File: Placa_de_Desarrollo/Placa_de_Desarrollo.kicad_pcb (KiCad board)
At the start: 2 copper layers, 1 part, among them U1 Pico

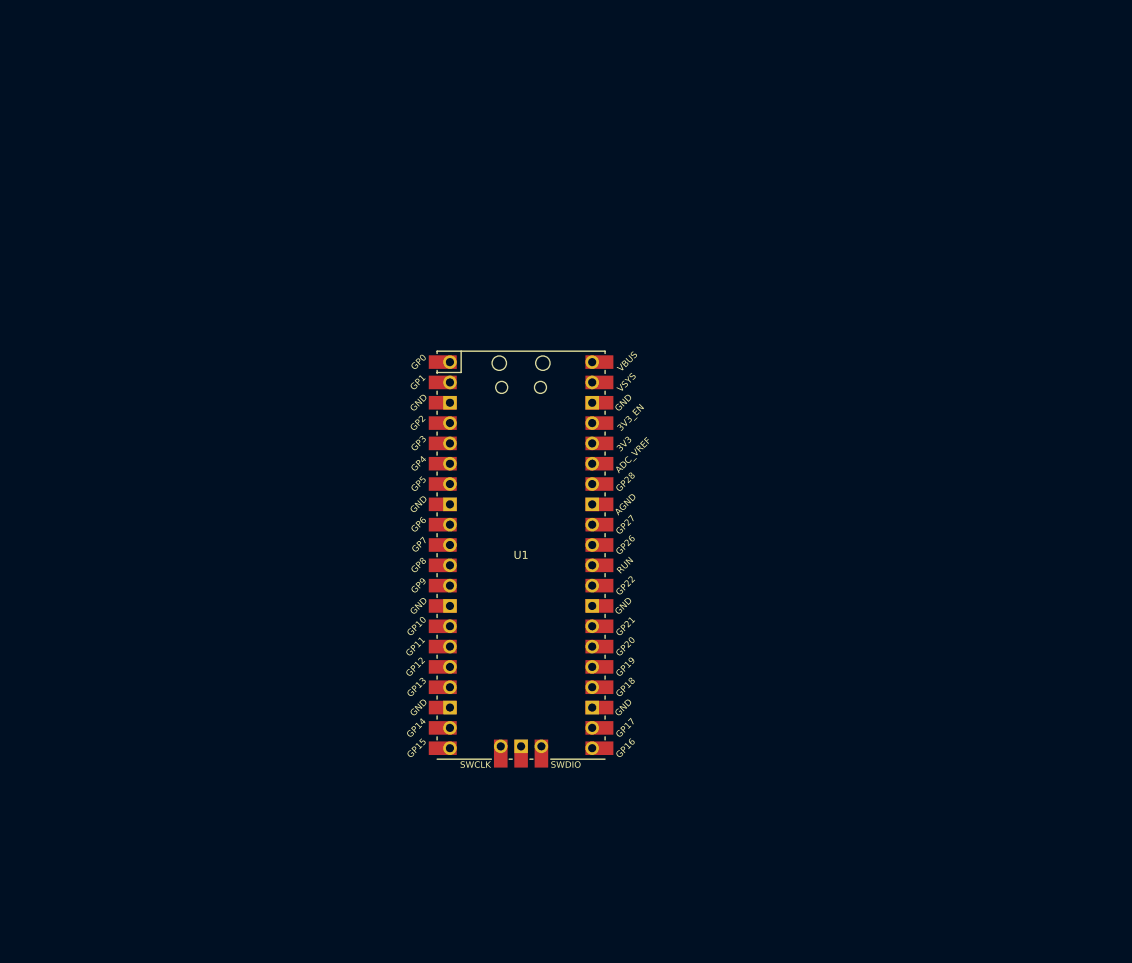
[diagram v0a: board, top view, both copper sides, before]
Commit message: Cambio de huella del Buzzer
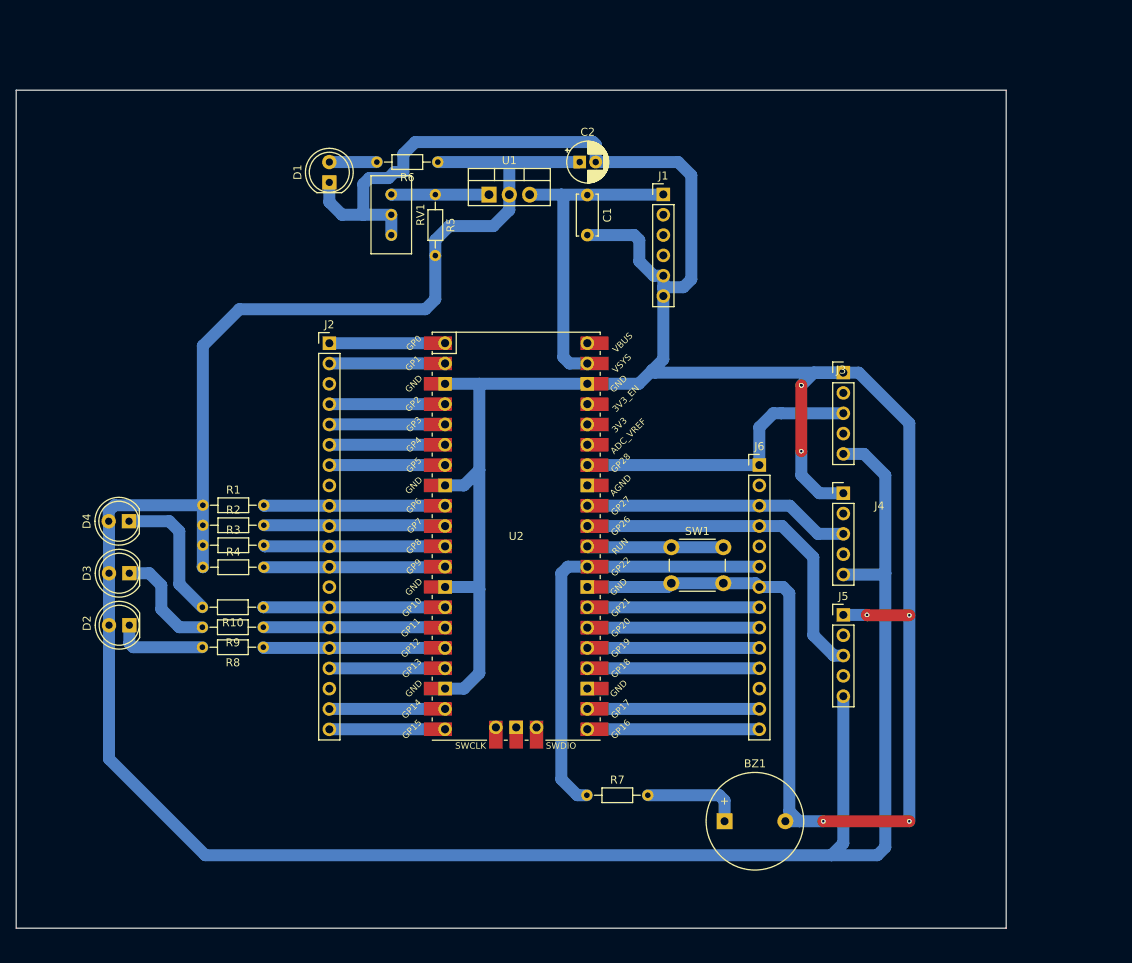
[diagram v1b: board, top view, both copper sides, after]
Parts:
- added BZ1: Buzzer, Buzzer_Beeper:Buzzer_12x9.5RM7.6, F.Cu at (172.0, 125.6)
- added C1: 0.1uF, Capacitor_THT:C_Disc_D5.0mm_W2.5mm_P5.00mm, F.Cu at (154.9, 47.4)
- added C2: 10uF, Capacitor_THT:CP_Radial_D5.0mm_P2.00mm, F.Cu at (153.9, 43.2)
- added D1: LED, LED_THT:LED_D5.0mm, F.Cu at (122.6, 45.8)
- added D2: LED, LED_THT:LED_D5.0mm, F.Cu at (97.6, 101.1)
- added D3: LED, LED_THT:LED_D5.0mm, F.Cu at (97.6, 94.6)
- added D4: LED, LED_THT:LED_D5.0mm, F.Cu at (97.6, 88.1)
- added J1: USB_B_Micro, Connector_PinHeader_2.54mm:PinHeader_1x06_P2.54mm_Vertical, F.Cu at (164.4, 47.3)
- added J2: Conn_01x20, Connector_PinHeader_2.54mm:PinHeader_1x20_P2.54mm_Vertical, F.Cu at (122.6, 65.9)
- added J3: ADC0, Connector_PinHeader_2.54mm:PinHeader_1x05_P2.54mm_Vertical, F.Cu at (186.9, 69.6)
- added J4: ADC1, Connector_PinHeader_2.54mm:PinHeader_1x05_P2.54mm_Vertical, F.Cu at (186.9, 84.6)
- added J5: ADC2, Connector_PinHeader_2.54mm:PinHeader_1x05_P2.54mm_Vertical, F.Cu at (186.9, 99.8)
- added J6: Conn_01x14, Connector_PinHeader_2.54mm:PinHeader_1x14_P2.54mm_Vertical, F.Cu at (176.4, 81.1)
- added R1: 4,7k, Resistor_THT:R_Axial_DIN0204_L3.6mm_D1.6mm_P7.62mm_Horizontal, F.Cu at (106.8, 86.1)
- added R10: 220, Resistor_THT:R_Axial_DIN0204_L3.6mm_D1.6mm_P7.62mm_Horizontal, F.Cu at (114.4, 98.9)
- added R2: 4,7k, Resistor_THT:R_Axial_DIN0204_L3.6mm_D1.6mm_P7.62mm_Horizontal, F.Cu at (106.8, 88.6)
- added R3: 4,7k, Resistor_THT:R_Axial_DIN0204_L3.6mm_D1.6mm_P7.62mm_Horizontal, F.Cu at (106.8, 91.1)
- added R4: 4,7k, Resistor_THT:R_Axial_DIN0204_L3.6mm_D1.6mm_P7.62mm_Horizontal, F.Cu at (106.8, 93.9)
- added R5: 240, Resistor_THT:R_Axial_DIN0204_L3.6mm_D1.6mm_P7.62mm_Horizontal, F.Cu at (135.9, 47.3)
- added R6: 240, Resistor_THT:R_Axial_DIN0204_L3.6mm_D1.6mm_P7.62mm_Horizontal, F.Cu at (136.2, 43.2)
- added R7: 100, Resistor_THT:R_Axial_DIN0204_L3.6mm_D1.6mm_P7.62mm_Horizontal, F.Cu at (154.8, 122.4)
- added R8: 220, Resistor_THT:R_Axial_DIN0204_L3.6mm_D1.6mm_P7.62mm_Horizontal, F.Cu at (114.4, 103.9)
- added R9: 220, Resistor_THT:R_Axial_DIN0204_L3.6mm_D1.6mm_P7.62mm_Horizontal, F.Cu at (114.4, 101.4)
- added RV1: 1K, Potentiometer_THT:Potentiometer_Bourns_3296W_Vertical, F.Cu at (130.4, 52.4)
- added SW1: RESET, Button_Switch_THT:SW_PUSH_6mm_H9.5mm, F.Cu at (165.4, 91.4)
- added U1: LM317_TO-220, Package_TO_SOT_THT:TO-220-3_Vertical, F.Cu at (142.6, 47.3)
- moved U2 2.45 mm to (146.0, 90.0)
- renumbered U1 to U2
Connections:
- U2 pad 1: unconnected-(U1-GPIO0-Pad1) -> GPIO0/SCK
- U2 pad 10: unconnected-(U1-GPIO7-Pad10) -> SCL1
- U2 pad 11: unconnected-(U1-GPIO8-Pad11) -> SDA0
- U2 pad 12: unconnected-(U1-GPIO9-Pad12) -> SCL0
- U2 pad 13: unconnected-(U1-GND-Pad13) -> GND
- U2 pad 14: unconnected-(U1-GPIO10-Pad14) -> LED1
- U2 pad 15: unconnected-(U1-GPIO11-Pad15) -> LED2
- U2 pad 16: unconnected-(U1-GPIO12-Pad16) -> LED3
- U2 pad 17: unconnected-(U1-GPIO13-Pad17) -> GPIO13
- U2 pad 18: unconnected-(U1-GND-Pad18) -> GND
- U2 pad 19: unconnected-(U1-GPIO14-Pad19) -> F1/GPIO14
- U2 pad 2: unconnected-(U1-GPIO1-Pad2) -> GPIO1/TX
- U2 pad 20: unconnected-(U1-GPIO15-Pad20) -> F2/GPIO15
- U2 pad 21: unconnected-(U1-GPIO16-Pad21) -> F3/GPIO16
- U2 pad 22: unconnected-(U1-GPIO17-Pad22) -> F4/GPIO17
- U2 pad 23: unconnected-(U1-GND-Pad23) -> GND
- U2 pad 24: unconnected-(U1-GPIO18-Pad24) -> C1/GPIO18
- U2 pad 25: unconnected-(U1-GPIO19-Pad25) -> C2/GPIO19
- U2 pad 26: unconnected-(U1-GPIO20-Pad26) -> C3/GPIO20
- U2 pad 27: unconnected-(U1-GPIO21-Pad27) -> C4/GPIO21
- U2 pad 28: unconnected-(U1-GND-Pad28) -> GND
- U2 pad 29: unconnected-(U1-GPIO22-Pad29) -> BUZZER
- U2 pad 3: unconnected-(U1-GND-Pad3) -> GND
- U2 pad 30: unconnected-(U1-RUN-Pad30) -> Net-(U2-RUN)
- U2 pad 31: unconnected-(U1-GPIO26_ADC0-Pad31) -> ADC0
- U2 pad 32: unconnected-(U1-GPIO27_ADC1-Pad32) -> ADC1
- U2 pad 34: unconnected-(U1-GPIO28_ADC2-Pad34) -> ADC2
- U2 pad 38: unconnected-(U1-GND-Pad38) -> GND
- U2 pad 39: unconnected-(U1-VSYS-Pad39) -> 5V
- U2 pad 4: unconnected-(U1-GPIO2-Pad4) -> GPIO2/RX
- U2 pad 5: unconnected-(U1-GPIO3-Pad5) -> GPIO3/CSn
- U2 pad 6: unconnected-(U1-GPIO4-Pad6) -> GPIO4
- U2 pad 7: unconnected-(U1-GPIO5-Pad7) -> GPIO5
- U2 pad 8: unconnected-(U1-GND-Pad8) -> GND
- U2 pad 9: unconnected-(U1-GPIO6-Pad9) -> SDA1
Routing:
- net GND: track 0.00 -> 371.3 mm, vias 0 -> 7
- net 3.3V: track 0.00 -> 325.3 mm
- net BUZZER: track 0.00 -> 54.9 mm
- net ADC0: track 0.00 -> 44.4 mm
- net 5V: track 0.00 -> 40.5 mm
- net ADC2: track 0.00 -> 37.5 mm
- net ADC1: track 0.00 -> 33.5 mm
- net LED3: track 0.00 -> 22.8 mm
- net LED2: track 0.00 -> 22.7 mm
- net LED1: track 0.00 -> 22.7 mm
- net SDA0: track 0.00 -> 22.7 mm
- net SCL1: track 0.00 -> 22.7 mm
- net SCL0: track 0.00 -> 22.7 mm
- net SDA1: track 0.00 -> 22.7 mm
- net C4/GPIO21: track 0.00 -> 21.5 mm
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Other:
- board outline added: 123.8 x 104.8 mm

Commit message: Mejora de Placa de desarrollo
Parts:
- removed J1: USB_B_Micro, Connector_PinHeader_2.54mm:PinHeader_1x06_P2.54mm_Vertical
- removed the J3 at (186.9, 69.6)
- removed J4: ADC1, Connector_PinHeader_2.54mm:PinHeader_1x05_P2.54mm_Vertical
- removed J5: ADC2, Connector_PinHeader_2.54mm:PinHeader_1x05_P2.54mm_Vertical
- added RV2: 10k, Potentiometer_THT:Potentiometer_Piher_T-16H_Single_Horizontal, F.Cu at (158.8, 43.4)
- added RV3: 10k, Potentiometer_THT:Potentiometer_Piher_T-16H_Single_Horizontal, F.Cu at (177.3, 43.4)
- added RV4: 10k, Potentiometer_THT:Potentiometer_Piher_T-16H_Single_Horizontal, F.Cu at (196.1, 43.4)
- added U3: ~, Micro_USB_PCB:Micro_USB_B, F.Cu at (124.9, 79.0)
- SW1: footprint Button_Switch_THT:SW_PUSH_6mm_H9.5mm -> Button_Switch_THT:SW_PUSH_6mm
- U2: value Pico -> RP2350; footprint MCU_RaspberryPi_and_Boards:RPi_Pico_SMD_TH -> BoardF_Pi_Pico:BoardF_Pi_Pico_RP2350
- moved R7 69.1 mm to (170.8, 55.1), turned to 180 degrees
- moved J2 59.4 mm to (148.1, 119.6), turned to 90 degrees
- moved BZ1 56.4 mm to (156.7, 71.4), turned to -90 degrees
- moved R1 42.1 mm to (128.5, 122.2)
- moved R2 42.0 mm to (128.5, 124.5)
- moved R3 41.9 mm to (128.5, 127.0)
- moved R4 41.5 mm to (128.5, 129.3)
- moved D4 41.2 mm to (121.6, 121.6)
- moved D2 41.2 mm to (121.7, 134.6)
- moved D3 41.2 mm to (121.7, 128.1)
- moved R10 39.5 mm to (136.1, 131.8)
- moved R9 39.3 mm to (136.1, 134.1)
- moved R8 39.1 mm to (136.1, 136.4)
- moved C1 32.8 mm to (130.1, 68.8), turned to 90 degrees
- moved D1 31.9 mm to (147.3, 66.0), turned to -90 degrees
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- renumbered J6 to J3
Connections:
- J2 pad 13: unconnected-(J2-Pin_13-Pad13) -> GND
- J2 pad 18: unconnected-(J2-Pin_18-Pad18) -> GND
- J2 pad 3: unconnected-(J2-Pin_3-Pad3) -> GND
- J2 pad 8: unconnected-(J2-Pin_8-Pad8) -> GND
- J3 pad 12: unconnected-(J6-Pin_12-Pad12) -> GND
- J3 pad 2: unconnected-(J6-Pin_2-Pad2) -> GND
- U2 pad 33: unconnected-(U2-AGND-Pad33)_0 -> GND
- U2 pad 42: unconnected-(U2-GND-Pad42) -> GND
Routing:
- net 3.3V: track 325.3 -> 236.1 mm
- net LED3: track 22.8 -> 72.5 mm
- net LED2: track 22.7 -> 69.0 mm
- net LED1: track 22.7 -> 65.5 mm
- net GND: track 371.3 -> 409.2 mm, vias 7 -> 0
- net SCL0: track 22.7 -> 59.4 mm
- net SDA0: track 22.7 -> 55.9 mm
- net SCL1: track 22.7 -> 52.3 mm
- net SDA1: track 22.7 -> 48.9 mm
- net BUZZER: track 54.9 -> 34.9 mm
- net ADC0: track 44.4 -> 62.4 mm
- net ADC2: track 37.5 -> 54.1 mm
- net ADC1: track 33.5 -> 44.6 mm
- net Net-(BZ1-+): track 12.5 -> 21.5 mm
- net Net-(D1-A): track 5.94 -> 14.5 mm
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- added copper zone on B.Cu, net GND
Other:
- board size 123.8 x 104.8 mm -> 97.2 x 104.8 mm
- board text added: "0.1uF"
- board text added: "100"
- board text added: "10k"
- board text added: "10uF"
- board text added: "1k"
- board text added: "220"
- board text added: "240"
- board text added: "4.7k"
- board text added: "ADC0"
- board text added: "ADC1"
- board text added: "ADC2"
- board text added: "GPIO0/SCK"
- board text added: "GPIO1/TX"
- board text added: "GPIO10"
- board text added: "GPIO10/LED1"
- board text added: "GPIO11"
- board text added: "GPIO11/LED2"
- board text added: "GPIO12"
- board text added: "GPIO12/LED3"
- board text added: "GPIO13"
- board text added: "GPIO14"
- board text added: "GPIO15"
- board text added: "GPIO16"
- board text added: "GPIO17"
- board text added: "GPIO18"
- board text added: "GPIO19"
- board text added: "GPIO2/RX"
- board text added: "GPIO20"
- board text added: "GPIO21"
- board text added: "GPIO22/BUZZER"
- board text added: "GPIO3/CSn"
- board text added: "GPIO4"
- board text added: "GPIO5"
- board text added: "GPIO6/SDA1"
- board text added: "GPIO7/SCL1"
- board text added: "GPIO8/SDA0"
- board text added: "GPIO9/SCL0"
- board text added: "RESET"

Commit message: Version 1.0 finalizada
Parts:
- removed U3: ~, Micro_USB_PCB:Micro_USB_B
- added J1: USB_A, Connector_USB:USB_A_Molex_67643_Horizontal, F.Cu at (126.9, 70.8)
- added JP1: Jumper_2_Bridged, Connector_PinHeader_2.54mm:PinHeader_1x02_P2.54mm_Vertical, F.Cu at (187.6, 130.2)
- added JP2: Jumper_2_Bridged, Connector_PinHeader_2.54mm:PinHeader_1x02_P2.54mm_Vertical, F.Cu at (183.7, 130.2)
- added JP3: Jumper_2_Bridged, Connector_PinHeader_2.54mm:PinHeader_1x02_P2.54mm_Vertical, F.Cu at (179.9, 130.2)
- J2: value Conn_01x20 -> LEFT
- J3: value Conn_01x14 -> RIGHT
- moved R5 17.8 mm to (128.2, 54.4)
- moved R6 17.8 mm to (127.9, 45.4)
- moved C1 17.8 mm to (115.9, 58.1)
- moved C2 17.8 mm to (117.9, 49.0)
- moved D1 17.8 mm to (133.2, 55.3)
- moved RV1 17.8 mm to (133.9, 50.2)
- moved U1 17.8 mm to (126.4, 58.0)
- moved BZ1 17.7 mm to (149.9, 55.1)
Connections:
- net C1/GPIO18 renamed GPIO18
- net C2/GPIO19 renamed GPIO19
- net C3/GPIO20 renamed GPIO20
- net C4/GPIO21 renamed GPIO21
- net F1/GPIO14 renamed GPIO14
- net F2/GPIO15 renamed GPIO15
- net F3/GPIO16 renamed GPIO16
- net F4/GPIO17 renamed GPIO17
- net GPIO0/SCK renamed GPIO0
- net GPIO1/TX renamed GPIO1
- net GPIO2/RX renamed GPIO2
- net GPIO3/CSn renamed GPIO3
- R10 pad 1: LED1 -> Net-(JP3-B)
- R8 pad 1: LED3 -> Net-(JP1-B)
- R9 pad 1: LED2 -> Net-(JP2-B)
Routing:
- net Net-(JP1-B): track 0.00 -> 54.3 mm
- net Net-(JP2-B): track 0.00 -> 49.5 mm
- net GND: track 409.2 -> 456.6 mm
- net LED3: track 72.5 -> 26.6 mm
- net Net-(JP3-B): track 0.00 -> 44.1 mm
- net LED2: track 69.0 -> 26.0 mm
- net LED1: track 65.5 -> 26.5 mm
- net 5V: track 37.4 -> 58.4 mm
- net 3.3V: track 236.1 -> 248.9 mm
- net Net-(BZ1-+): track 21.5 -> 13.3 mm
- net SCL1: track 52.3 -> 54.4 mm
- net SDA0: track 55.9 -> 58.0 mm
- net SCL0: track 59.4 -> 61.3 mm
- net Net-(D3-K): track 9.34 -> 10.4 mm
- net SDA1: track 48.9 -> 50.0 mm
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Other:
- board text added: "GPIO0"
- board text added: "GPIO1"
- board text added: "GPIO2"
- board text added: "GPIO22/BZ"
- board text added: "GPIO3"
- board text removed: "GPIO0/SCK"
- board text removed: "GPIO1/TX"
- board text removed: "GPIO10/LED1"
- board text removed: "GPIO11/LED2"
- board text removed: "GPIO12/LED3"
- board text removed: "GPIO2/RX"
- board text removed: "GPIO22/BUZZER"
- board text removed: "GPIO3/CSn"

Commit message: Version 2.0 de la Placa de DEsarrollo
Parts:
- removed JP1, JP2, JP3: Jumper_2_Bridged, Connector_PinHeader_2.54mm:PinHeader_1x02_P2.54mm_Vertical
- removed RV1: 1K, Potentiometer_THT:Potentiometer_Bourns_3296W_Vertical
- removed U1: LM317_TO-220, Package_TO_SOT_THT:TO-220-3_Vertical
- added C3: 100nF, Capacitor_THT:C_Disc_D8.0mm_W2.5mm_P5.00mm, F.Cu at (198.6, 98.1)
- added J10: Conn_01x04, Connector_PinHeader_2.54mm:PinHeader_1x04_P2.54mm_Vertical, F.Cu at (131.9, 84.8)
- added J11: Conn_01x03, Connector_PinHeader_2.54mm:PinHeader_1x03_P2.54mm_Vertical, F.Cu at (193.6, 81.8)
- added J12: Conn_01x04, Connector_PinHeader_2.54mm:PinHeader_1x04_P2.54mm_Vertical, F.Cu at (131.9, 89.4)
- added J13: Conn_01x04, Connector_PinHeader_2.54mm:PinHeader_1x04_P2.54mm_Vertical, F.Cu at (183.9, 51.4)
- added J14: Conn_01x04, Connector_PinHeader_2.54mm:PinHeader_1x04_P2.54mm_Vertical, F.Cu at (183.9, 64.2)
- added J15: Conn_01x04, Connector_PinHeader_2.54mm:PinHeader_1x04_P2.54mm_Vertical, F.Cu at (183.7, 101.7)
- added J16: Conn_01x04, Connector_PinHeader_2.54mm:PinHeader_1x04_P2.54mm_Vertical, F.Cu at (183.6, 87.8)
- added J17: Conn_01x01, Connector_PinHeader_2.54mm:PinHeader_1x01_P2.54mm_Vertical, F.Cu at (144.0, 108.8)
- added J18: Conn_01x01, Connector_PinHeader_2.54mm:PinHeader_1x01_P2.54mm_Vertical, F.Cu at (183.7, 97.5)
- added J4: Conn_01x01, Connector_PinHeader_2.54mm:PinHeader_1x01_P2.54mm_Vertical, F.Cu at (169.2, 34.7)
- added J5: Conn_01x04, Connector_PinHeader_2.54mm:PinHeader_1x04_P2.54mm_Vertical, F.Cu at (125.6, 71.6)
- added J6: Conn_01x04, Connector_PinHeader_2.54mm:PinHeader_1x04_P2.54mm_Vertical, F.Cu at (130.8, 71.6)
- added J7: Conn_01x04, Connector_PinHeader_2.54mm:PinHeader_1x04_P2.54mm_Vertical, F.Cu at (124.3, 62.2)
- added J8: Conn_01x03, Connector_PinHeader_2.54mm:PinHeader_1x03_P2.54mm_Vertical, F.Cu at (121.4, 97.5)
- added J9: Conn_01x04, Connector_PinHeader_2.54mm:PinHeader_1x04_P2.54mm_Vertical, F.Cu at (124.3, 66.4)
- added Q1: BC547, Package_TO_SOT_THT:TO-92_Inline, F.Cu at (181.6, 41.0)
- added SW2: ´PULL DOWN, Button_Switch_THT:SW_PUSH_6mm, F.Cu at (178.6, 108.8)
- added SW3: PULL UP, Button_Switch_THT:SW_PUSH_6mm, F.Cu at (149.4, 104.2)
- C1: value 0.1uF -> 100nF; footprint Capacitor_THT:C_Disc_D5.0mm_W2.5mm_P5.00mm -> Capacitor_THT:C_Disc_D8.0mm_W2.5mm_P5.00mm
- C2: value 10uF -> 100nF; footprint Capacitor_THT:CP_Radial_D5.0mm_P2.00mm -> Capacitor_THT:C_Disc_D8.0mm_W2.5mm_P5.00mm
- D1: value LED -> 1N4007; footprint LED_THT:LED_D5.0mm -> Diode_THT:D_DO-41_SOD81_P10.16mm_Horizontal
- J3: footprint Connector_PinHeader_2.54mm:PinHeader_1x14_P2.54mm_Vertical -> Connector_PinHeader_2.54mm:PinHeader_1x20_P2.54mm_Vertical
- R5, R6: value 240 -> 10K
- R7: value 100 -> 1K
- moved C2 86.2 mm to (198.6, 79.3), turned to 90 degrees
- moved J1 84.2 mm to (207.5, 46.4), turned to 180 degrees
- moved C1 82.7 mm to (198.6, 60.9)
- moved J2 68.4 mm to (143.2, 51.3), turned to 0 degrees
- moved R5 67.3 mm to (167.8, 108.8)
- moved R6 67.1 mm to (160.2, 104.2)
- moved RV4 60.7 mm to (207.5, 103.1), turned to 0 degrees
- moved RV2 53.5 mm to (207.5, 65.9), turned to 0 degrees
- moved R1 53.1 mm to (111.1, 72.0)
- moved R3 53.1 mm to (111.1, 76.8)
- moved R4 53.1 mm to (111.1, 79.1)
- moved R2 53.1 mm to (111.1, 74.4)
- moved D1 51.0 mm to (177.0, 29.2)
- moved RV3 50.8 mm to (207.5, 84.3), turned to 0 degrees
- moved BZ1 44.2 mm to (185.7, 29.2)
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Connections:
- net LED1 renamed GPIO10
- net LED2 renamed GPIO11
- net LED3 renamed GPIO12
- BZ1 pad 1: Net-(BZ1-+) -> 5V
- BZ1 pad 2: GND -> Net-(BZ1--)
- C1 pad 1: 5V -> ADC0
- C2 pad 1: 3.3V -> ADC1
- D1 pad 1: GND -> 5V
- D1 pad 2: Net-(D1-A) -> Net-(BZ1--)
- J3 pad 1: ADC2 -> VBUS
- J3 pad 10: GPIO19 -> GPIO26
- J3 pad 11: GPIO18 -> RESET
- J3 pad 12: GND -> GPIO22
- J3 pad 13: GPIO17 -> GND
- J3 pad 14: GPIO16 -> GPIO21
- J3 pad 2: GND -> 5V
- J3 pad 3: ADC1 -> GND
- J3 pad 4: ADC0 -> 3V3_EB
- J3 pad 5: unconnected-(J3-Pin_5-Pad5) -> 3.3V
- J3 pad 6: BUZZER -> ADC_REF
- J3 pad 7: GND -> GPIO28
- J3 pad 8: GPIO21 -> GND
- J3 pad 9: GPIO20 -> GPIO27
- R5 pad 1: Net-(U1-ADJ) -> 3.3V
- R5 pad 2: 3.3V -> Net-(J17-Pin_1)
- R6 pad 1: 3.3V -> GND
- R6 pad 2: Net-(D1-A) -> Net-(J18-Pin_1)
- R7 pad 1: BUZZER -> Net-(J4-Pin_1)
- R7 pad 2: Net-(BZ1-+) -> Net-(Q1-B)
- RV2 pad 2: ADC2 -> ADC0
- RV4 pad 2: ADC0 -> ADC2
- SW1 pad 1: Net-(U2-RUN) -> RESET
- U2 pad 29: BUZZER -> GPIO22
- U2 pad 30: Net-(U2-RUN) -> RESET
- U2 pad 31: ADC0 -> GPIO26
- U2 pad 32: ADC1 -> GPIO27
- U2 pad 34: ADC2 -> GPIO28
- U2 pad 35: unconnected-(U2-ADC_REF-Pad35) -> ADC_REF
- U2 pad 36: unconnected-(U2-3V3_OUT-Pad36) -> 3.3V
- U2 pad 37: unconnected-(U2-3V3_EB-Pad37) -> 3V3_EB
- U2 pad 40: unconnected-(U2-VBUS-Pad40) -> VBUS
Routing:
- net 5V: track 58.4 -> 312.1 mm
- net Net-(J8-Pin_3): track 54.3 -> 2.99 mm
- net Net-(J8-Pin_2): track 49.5 -> 2.99 mm
- net Net-(J8-Pin_1): track 44.1 -> 3.01 mm
- net BUZZER: track 34.8 -> 0.00 mm
- net ADC0: track 62.4 -> 28.2 mm
- net ADC1: track 44.6 -> 13.9 mm
- net SCL0: track 61.3 -> 31.1 mm
- net SDA0: track 58.0 -> 31.1 mm
- net 3.3V: track 248.9 -> 275.1 mm
- net ADC2: track 54.1 -> 28.6 mm
- net SCL1: track 54.4 -> 31.1 mm
- net Net-(J18-Pin_1): track 0.00 -> 21.6 mm
- net GPIO12: track 26.6 -> 6.51 mm
- net GPIO10: track 26.5 -> 6.51 mm
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- removed copper zone on B.Cu, net GND
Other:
- board size 97.2 x 104.8 mm -> 115 x 95 mm
- board text added: "5V"
- board text added: "BUZZER"
- board text added: "GND"
- board text added: "GP0"
- board text added: "GP1"
- board text added: "GP10"
- board text added: "GP11"
- board text added: "GP12"
- board text added: "GP13"
- board text added: "GP14"
- board text added: "GP15"
- board text added: "GP16"
- board text added: "GP17"
- board text added: "GP18"
- board text added: "GP19"
- board text added: "GP2"
- board text added: "GP20"
- board text added: "GP21"
- board text added: "GP22"
- board text added: "GP3"
- board text added: "GP4"
- board text added: "GP5"
- board text added: "GP6"
- board text added: "GP7"
- board text added: "GP8"
- board text added: "GP9"
- board text added: "LED"
- board text added: "POWER"
- board text added: "PULL DOWN"
- board text added: "PULL UP"
- board text added: "SCL0"
- board text added: "SCL1"
- board text added: "SDA0"
- board text added: "SDA1"
- board text removed: "0.1uF"
- board text removed: "100"
- board text removed: "10uF"
- board text removed: "1k"
- board text removed: "220"
- board text removed: "240"
- board text removed: "GPIO0"
- board text removed: "GPIO1"
- board text removed: "GPIO10"
- board text removed: "GPIO11"
- board text removed: "GPIO12"
- board text removed: "GPIO13"
- board text removed: "GPIO14"
- board text removed: "GPIO15"
- board text removed: "GPIO16"
- board text removed: "GPIO17"
- board text removed: "GPIO18"
- board text removed: "GPIO19"
- board text removed: "GPIO2"
- board text removed: "GPIO20"
- board text removed: "GPIO21"
- board text removed: "GPIO22/BZ"
- board text removed: "GPIO3"
- board text removed: "GPIO4"
- board text removed: "GPIO5"
- board text removed: "GPIO6/SDA1"
- board text removed: "GPIO7/SCL1"
- board text removed: "GPIO8/SDA0"
- board text removed: "GPIO9/SCL0"

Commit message: Actualizacion de rama
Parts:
- SW2: value ´PULL DOWN -> PULL DOWN
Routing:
- net 3.3V: track 275.1 -> 284.1 mm
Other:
- board text added: "3.3V"
- board text added: "ADC"
- board text added: "REF"
